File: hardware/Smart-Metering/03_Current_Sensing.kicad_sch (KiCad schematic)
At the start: 0 parts

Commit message: Implementa front-ends de tensão e corrente do ADE9430
02_Voltage_Sensing (3 fases, pseudo-diferencial):
- borne J101 (VA/VB/VC/VN) com labels globais LINE_A/B/C e NEUTRAL;
- fusível + varistor 320 VAC fase-neutro por fase;
- divisor 5 x 200 kΩ + 1 kΩ (1/1001): 220 V -> 0,311 Vpk, até ~354 Vrms
  com no máximo 0,5 Vpk por pino (limite do ADE9430: ±0,6 V);
- anti-aliasing 999 Ω // 22 nF (fc ≈ 7,2 kHz); VxN com 1 kΩ // 22 nF
  para casar impedância;
- R101 (0 Ω) liga NEUTRAL ao GND metrológico em ponto único.

03_Current_Sensing (IA/IB/IC/IN):
- entrada de TC por borne de 2 vias, TVS bidirecional SMAJ5.0CA;
- burden 2 x 10 Ω com center-tap no GND (TC 2500:1 -> fundo de escala
  ≈ 88 Arms, ±0,5 Vpk por pino);
- anti-aliasing 1 kΩ + 22 nF por perna (fc ≈ 7,2 kHz, casado com a tensão).

Biblioteca: novos símbolos Fuse, Varistor, D_TVS_Bi e
Screw_Terminal_01x02/01x04, já na convenção Y para cima do KiCad.

Co-Authored-By: Claude Opus 5.5 <noreply@anthropic.com>
Claude-Session: https://claude.ai/code/session_012B8cVkhtjf3eg98UdpNCpf
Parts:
- added C211, C212, C221, C222, C231, C232, C241, C242: 22nF C0G, Capacitor_SMD:C_0603_1608Metric, symbol SmartMetering:C_Vert
- added D201, D202, D203, D204: SMAJ5.0CA, Diode_SMD:D_SMA, symbol SmartMetering:D_TVS_Bi
- added J201: CT_IA, TerminalBlock_Phoenix:TerminalBlock_Phoenix_MKDS-1,5-2-5.08_1x02_P5.08mm_Horizontal, symbol SmartMetering:Screw_Terminal_01x02
- added J202: CT_IB, TerminalBlock_Phoenix:TerminalBlock_Phoenix_MKDS-1,5-2-5.08_1x02_P5.08mm_Horizontal, symbol SmartMetering:Screw_Terminal_01x02
- added J203: CT_IC, TerminalBlock_Phoenix:TerminalBlock_Phoenix_MKDS-1,5-2-5.08_1x02_P5.08mm_Horizontal, symbol SmartMetering:Screw_Terminal_01x02
- added J204: CT_IN, TerminalBlock_Phoenix:TerminalBlock_Phoenix_MKDS-1,5-2-5.08_1x02_P5.08mm_Horizontal, symbol SmartMetering:Screw_Terminal_01x02
- added R211, R212, R221, R222, R231, R232, R241, R242: 10R 0.1%, Resistor_SMD:R_1206_3216Metric, symbol SmartMetering:R_Vert
- added R213, R214, R223, R224, R233, R234, R243, R244: 1k 0.1%, Resistor_SMD:R_0603_1608Metric, symbol SmartMetering:R_Vert
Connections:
- new net: D202.1, J202.1, R221.1, R223.1
- new net: D202.2, J202.2, R222.2, R224.1
- new net: D203.1, J203.1, R231.1, R233.1
- new net: D203.2, J203.2, R232.2, R234.1
- new net: D201.2, J201.2, R212.2, R214.1
- new net: D204.1, J204.1, R241.1, R243.1
- new net: D204.2, J204.2, R242.2, R244.1
- new net: D201.1, J201.1, R211.1, R213.1
- new net GND: C211.1, C212.2, C221.1, C222.2, C231.1, C232.2, C241.1, C242.2, R211.2, R212.1, R221.2, R222.1, R231.2, R232.1, R241.2, R242.1
- new net IAN: C212.1, R214.2
- new net IAP: C211.2, R213.2
- new net IBN: C222.1, R224.2
- new net IBP: C221.2, R223.2
- new net ICN: C232.1, R234.2
- new net ICP: C231.2, R233.2
- new net INN: C242.1, R244.2
- new net INP: C241.2, R243.2
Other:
- note added: "FRONT-END DE CORRENTE — TC COM SAÍDA EM CORRENTE, DIFERENCIAL TC de referência: 2500:1 (mesma relação do EVAL-ADE9430) Burden: 2 x 10 Ω com center-tap no GND -> sinais IxP/IxN em antifase Fundo de escala do ADC: ±1 Vpk diferencial = 0,707 Vrms 0,707 V / 20 Ω = 35,4 mA no secundário -> Ifs ≈ 88 Arms no primário No fundo de escala cada pino fica em ±0,5 Vpk (limite ±0,6 V) Outra faixa: Rb_total = 0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"
- note added: "IA"
- note added: "IB"
- note added: "IC"
- note added: "IN (opcional)"
- company: (none) -> Smart-Metering
- title: (none) -> Current Sensing - ADE9430 Front-End

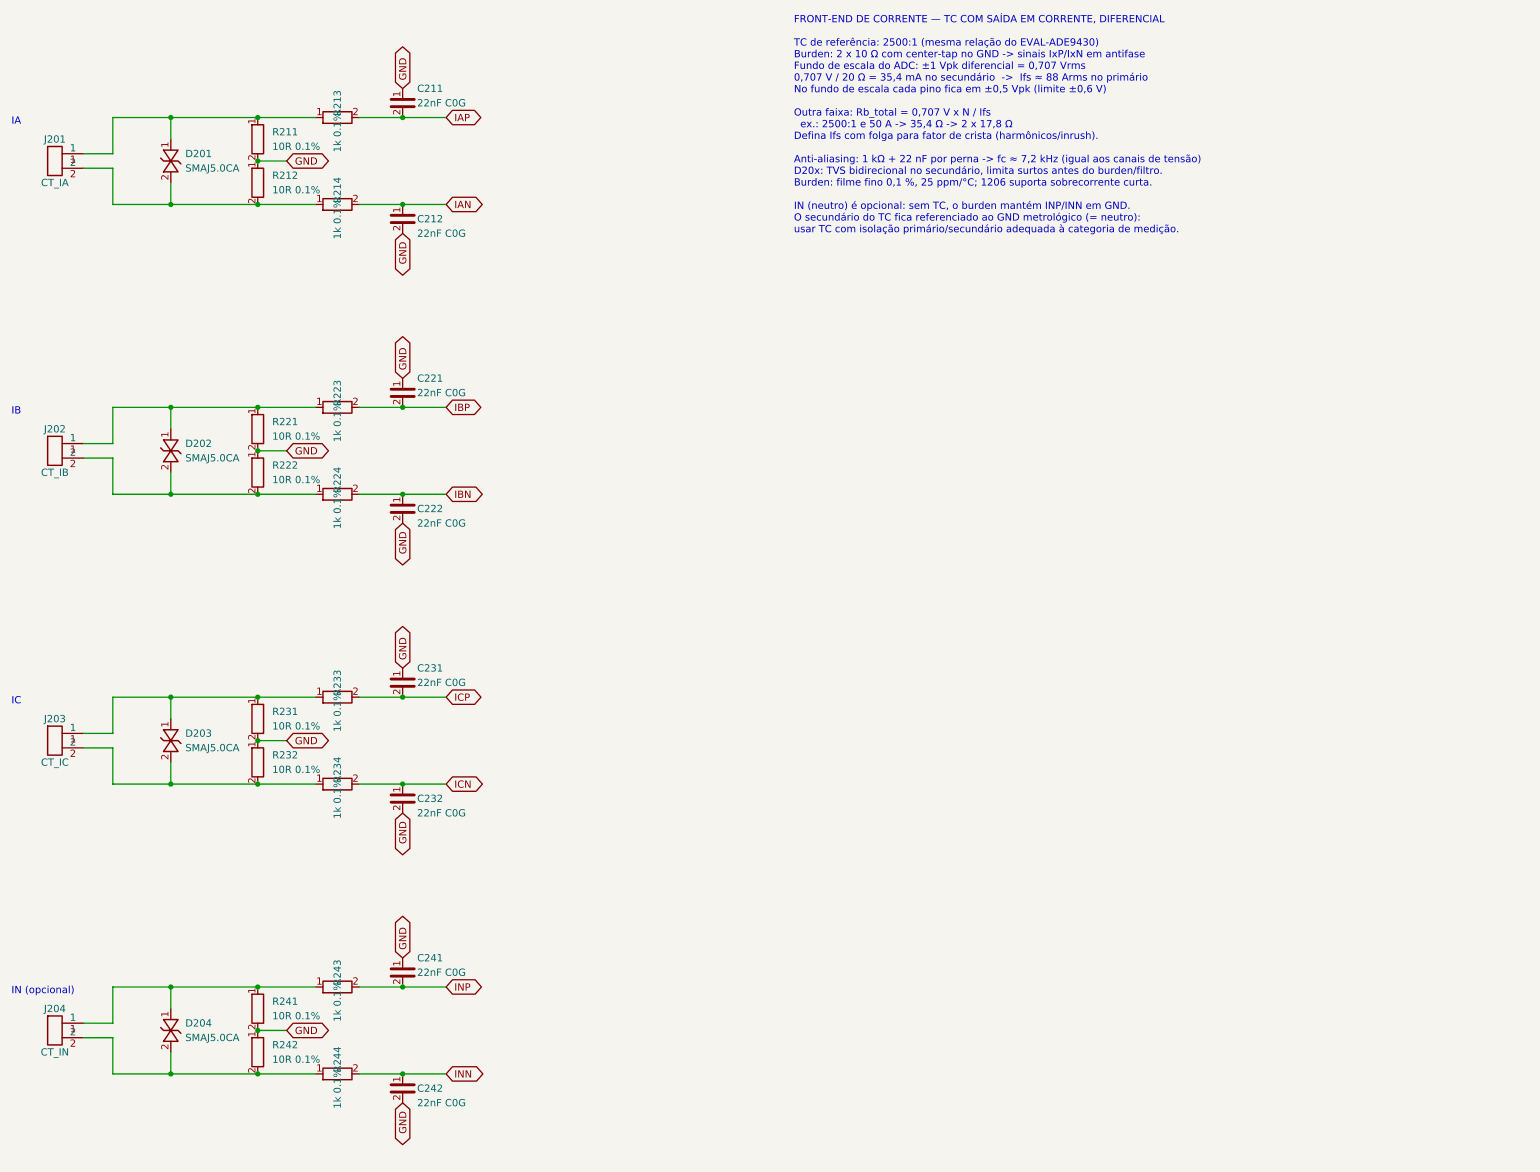
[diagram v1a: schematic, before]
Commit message: Refaz entrada de corrente para sensores configuráveis por montagem
A folha 03_Current_Sensing deixa de usar TC com saída em corrente
(risco de secundário aberto ao desconectar) e passa a aceitar, na
mesma placa, três tipos de sensor escolhidos pelos valores de Ra/Rb:

- TC 333 mV (padrão): Ra = 1k, Rb = 1M, ADE9430 com PGA 1x;
- bobina Rogowski: Ra = 1k, Rb = 1M, PGA 4x e integrador digital;
- SCT-013 com saída de 1 V (protótipo): Ra = 2k49, Rb = 1k65 (x0,40).

Em todas as opções Ra // Rb ≈ 1 kΩ, mantendo o anti-aliasing de
7,2 kHz com 22 nF, casado com os canais de tensão. Rb para GND em cada
perna referencia o sensor flutuante de forma simétrica.

Conector do sensor com 4 vias (S+, ID, GND, S-): o pino ID recebe um
pull-up de 10 kΩ para +3V3_ADE e filtro de 100 nF, saindo como SID_x
para leitura no domínio metrológico (a definir em 06_Isolation).

Biblioteca: novo símbolo genérico Conn_01x04.

Co-Authored-By: Claude Opus 5.5 <noreply@anthropic.com>
Claude-Session: https://claude.ai/code/session_012B8cVkhtjf3eg98UdpNCpf
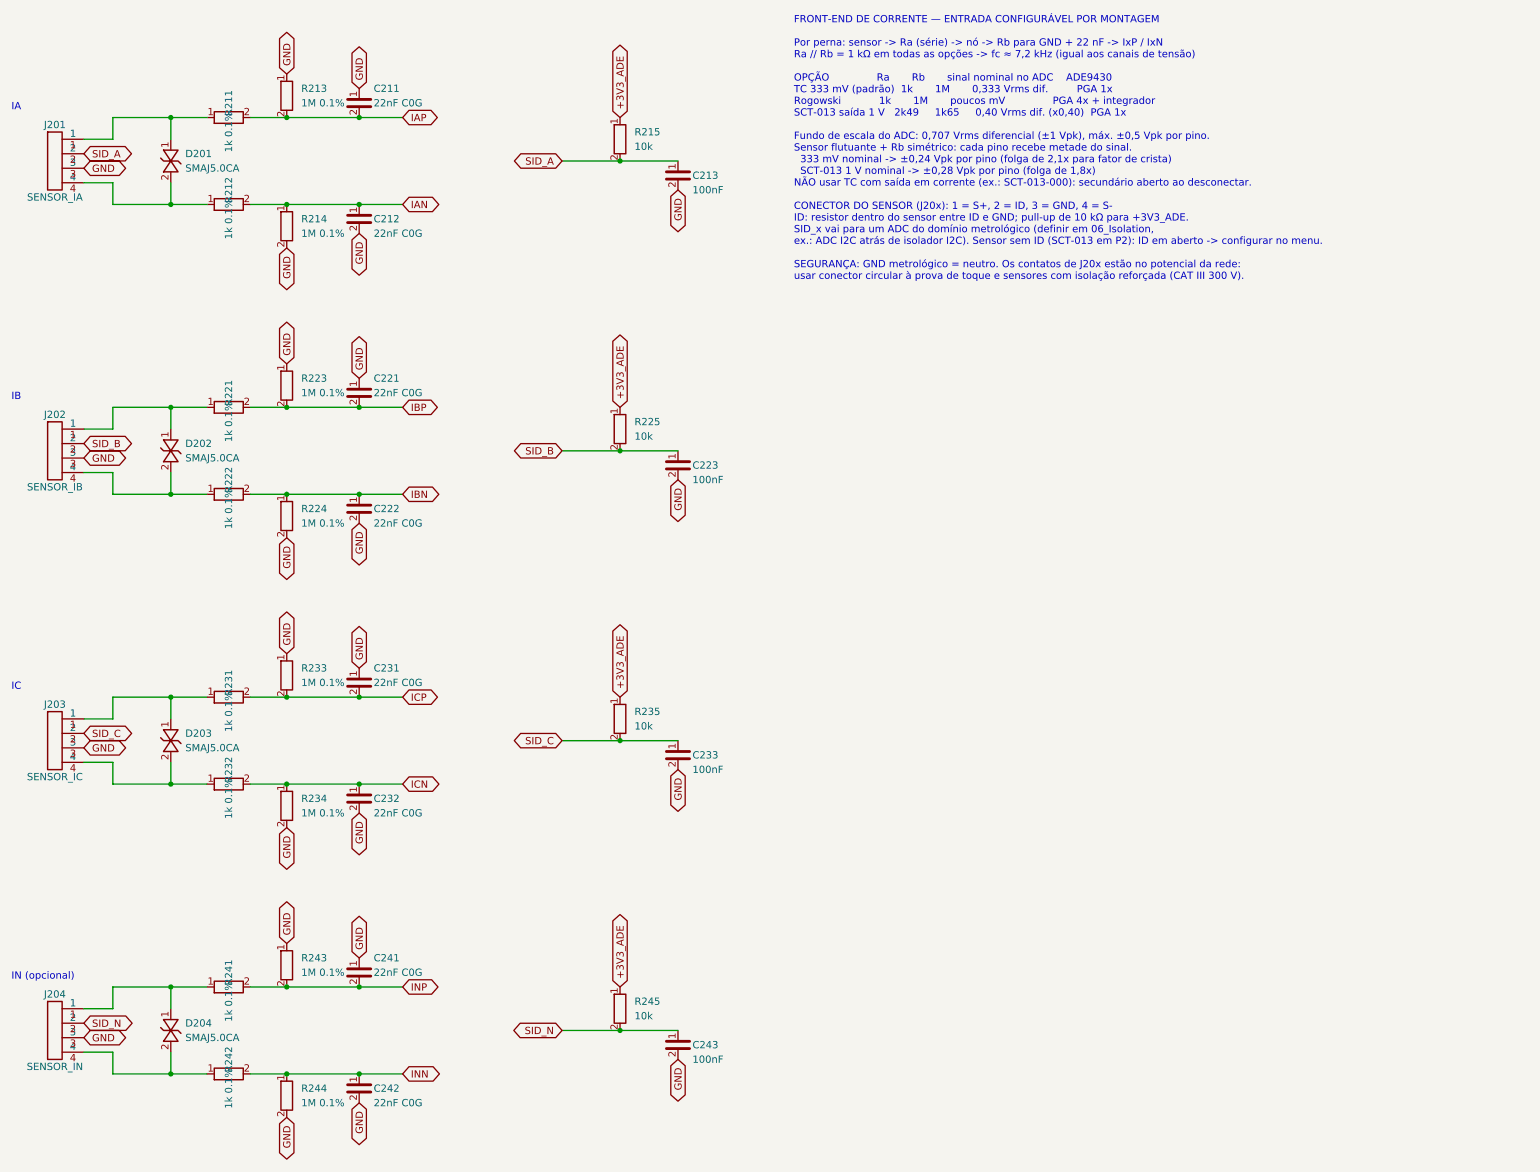
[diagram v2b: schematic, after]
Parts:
- removed J201: CT_IA, TerminalBlock_Phoenix:TerminalBlock_Phoenix_MKDS-1,5-2-5.08_1x02_P5.08mm_Horizontal, symbol SmartMetering:Screw_Terminal_01x02
- removed J202: CT_IB, TerminalBlock_Phoenix:TerminalBlock_Phoenix_MKDS-1,5-2-5.08_1x02_P5.08mm_Horizontal, symbol SmartMetering:Screw_Terminal_01x02
- removed J203: CT_IC, TerminalBlock_Phoenix:TerminalBlock_Phoenix_MKDS-1,5-2-5.08_1x02_P5.08mm_Horizontal, symbol SmartMetering:Screw_Terminal_01x02
- removed J204: CT_IN, TerminalBlock_Phoenix:TerminalBlock_Phoenix_MKDS-1,5-2-5.08_1x02_P5.08mm_Horizontal, symbol SmartMetering:Screw_Terminal_01x02
- added C213, C223, C233, C243: 100nF, Capacitor_SMD:C_0603_1608Metric, symbol SmartMetering:C_Vert
- added J201: SENSOR_IA, symbol SmartMetering:Conn_01x04
- added J202: SENSOR_IB, symbol SmartMetering:Conn_01x04
- added J203: SENSOR_IC, symbol SmartMetering:Conn_01x04
- added J204: SENSOR_IN, symbol SmartMetering:Conn_01x04
- added R215, R225, R235, R245: 10k, Resistor_SMD:R_0603_1608Metric, symbol SmartMetering:R_Vert
- R211, R212, R221, R222, R231, R232, R241, R242: value 10R 0.1% -> 1k 0.1%; footprint Resistor_SMD:R_1206_3216Metric -> Resistor_SMD:R_0603_1608Metric
- R213, R214, R223, R224, R233, R234, R243, R244: value 1k 0.1% -> 1M 0.1%
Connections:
- net GND: now also R213.1, R214.2, R223.1, R224.2, R233.1, R234.2, R243.1, R244.2, C213.2, C223.2, C233.2, C243.2, J201.3, J202.3, J203.3, J204.3; no longer R211.2, R212.1, R221.2, R222.1, R231.2, R232.1, R241.2, R242.1
- net IAN: now also R212.2, R214.1; no longer R214.2
- net IAP: now also R211.2
- net IBN: now also R222.2, R224.1; no longer R224.2
- net IBP: now also R221.2
- net ICN: now also R232.2, R234.1; no longer R234.2
- net ICP: now also R231.2
- net INN: now also R242.2, R244.1; no longer R244.2
- net INP: now also R241.2
- net at D202.1, R221.1: now also J202.1; no longer R223.1
- net at D203.1, R231.1: now also J203.1; no longer R233.1
- net at D204.1, R241.1: now also J204.1; no longer R243.1
- net at D201.1, R211.1: now also J201.1; no longer R213.1
- new net: D203.2, J203.4, R232.1
- new net: D204.2, J204.4, R242.1
- new net: D202.2, J202.4, R222.1
- new net: D201.2, J201.4, R212.1
- new net +3V3_ADE: R215.1, R225.1, R235.1, R245.1
- new net SID_A: C213.1, J201.2, R215.2
- new net SID_B: C223.1, J202.2, R225.2
- new net SID_C: C233.1, J203.2, R235.2
- new net SID_N: C243.1, J204.2, R245.2
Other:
- note added: "FRONT-END DE CORRENTE — ENTRADA CONFIGURÁVEL POR MONTAGEM Por perna: sensor -> Ra (série) -> nó -> Rb para GND + 22 nF -> IxP / IxN Ra // Rb = 1 kΩ em todas as opções -> fc ≈ 7,2 kHz (igual aos canais de tensão) OPÇÃO Ra Rb sinal nominal no ADC ADE9430 TC 333 mV (padrão) 1k 1M 0,333 Vrms dif. PGA 1x Rogowski 1k 1M poucos mV PGA 4x + integrador SCT-013 saída 1 V 2k49 1k65 0,40 Vrms dif. (x0,40) PG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"
- note removed: "FRONT-END DE CORRENTE — TC COM SAÍDA EM CORRENTE, DIFERENCIAL TC de referência: 2500:1 (mesma relação do EVAL-ADE9430) Burden: 2 x 10 Ω com center-tap no GND -> sinais IxP/IxN em antifase Fundo de escala do ADC: ±1 Vpk diferencial = 0,707 Vrms 0,707 V / 20 Ω = 35,4 mA no secundário -> Ifs ≈ 88 Arms no primário No fundo de escala cada pino fica em ±0,5 Vpk (limite ±0,6 V) Outra faixa: Rb_total = 0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"

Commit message: Implementa folha de entrada de energia e numera referências por folha
01_Power_Input:
- modo padrão: LINE_A/B/C -> fusível -> diodo S1M em OU para o
  barramento HV, retorno no NEUTRAL via JP101; o instrumento segue
  alimentado com qualquer fase presente;
- modo auxiliar (J101, 100-240 VAC, com varistor): F104/D104/JP102,
  não montados por padrão; para rede 3 fios sem neutro;
- R101 fusível limita inrush, C101 4,7 uF/450 V no barramento;
- PS101 módulo AC/DC isolado 5 V / 2 A (ex.: IRM-10-5) gerando
  VIN_ACDC para a folha 09, referenciado a GND_SYS.

Referências renumeradas por folha para evitar colisões: folha 02 passa
a 2xx (R201 = ligação neutro/GND), folha 03 a 3xx e folha 04 a 4xx
(U401 = ADE9430).

Novos símbolos: D_Rect, CP_Vert, Jumper_2 e ACDC_Module.

Co-Authored-By: Claude Opus 5.5 <noreply@anthropic.com>
Claude-Session: https://claude.ai/code/session_012B8cVkhtjf3eg98UdpNCpf
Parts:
- removed C211, C212, C221, C222, C231, C232, C241, C242: 22nF C0G, Capacitor_SMD:C_0603_1608Metric, symbol SmartMetering:C_Vert
- removed C213, C223, C233, C243: 100nF, Capacitor_SMD:C_0603_1608Metric, symbol SmartMetering:C_Vert
- removed D201, D202, D203, D204: SMAJ5.0CA, Diode_SMD:D_SMA, symbol SmartMetering:D_TVS_Bi
- removed J201: SENSOR_IA, symbol SmartMetering:Conn_01x04
- removed J202: SENSOR_IB, symbol SmartMetering:Conn_01x04
- removed J203: SENSOR_IC, symbol SmartMetering:Conn_01x04
- removed J204: SENSOR_IN, symbol SmartMetering:Conn_01x04
- removed R211, R212, R221, R222, R231, R232, R241, R242: 1k 0.1%, Resistor_SMD:R_0603_1608Metric, symbol SmartMetering:R_Vert
- removed R213, R214, R223, R224, R233, R234, R243, R244: 1M 0.1%, Resistor_SMD:R_0603_1608Metric, symbol SmartMetering:R_Vert
- removed R215, R225, R235, R245: 10k, Resistor_SMD:R_0603_1608Metric, symbol SmartMetering:R_Vert
- added C311, C312, C321, C322, C331, C332, C341, C342: 22nF C0G, Capacitor_SMD:C_0603_1608Metric, symbol SmartMetering:C_Vert
- added C313, C323, C333, C343: 100nF, Capacitor_SMD:C_0603_1608Metric, symbol SmartMetering:C_Vert
- added D301, D302, D303, D304: SMAJ5.0CA, Diode_SMD:D_SMA, symbol SmartMetering:D_TVS_Bi
- added J301: SENSOR_IA, symbol SmartMetering:Conn_01x04
- added J302: SENSOR_IB, symbol SmartMetering:Conn_01x04
- added J303: SENSOR_IC, symbol SmartMetering:Conn_01x04
- added J304: SENSOR_IN, symbol SmartMetering:Conn_01x04
- added R311, R312, R321, R322, R331, R332, R341, R342: 1k 0.1%, Resistor_SMD:R_0603_1608Metric, symbol SmartMetering:R_Vert
- added R313, R314, R323, R324, R333, R334, R343, R344: 1M 0.1%, Resistor_SMD:R_0603_1608Metric, symbol SmartMetering:R_Vert
- added R315, R325, R335, R345: 10k, Resistor_SMD:R_0603_1608Metric, symbol SmartMetering:R_Vert
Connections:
- net +3V3_ADE: now also R315.1, R325.1, R335.1, R345.1
- net GND: now also C311.1, C312.2, C313.2, C321.1, C322.2, C323.2, C331.1, C332.2, C333.2, C341.1, C342.2, C343.2, J301.3, J302.3, J303.3, J304.3, R313.1, R314.2, R323.1, R324.2, R333.1, R334.2, R343.1, R344.2
- net IAN: now also C312.1, R312.2, R314.1
- net IAP: now also C311.2, R311.2, R313.2
- net IBN: now also C322.1, R322.2, R324.1
- net IBP: now also C321.2, R321.2, R323.2
- net ICN: now also C332.1, R332.2, R334.1
- net ICP: now also C331.2, R331.2, R333.2
- net INN: now also C342.1, R342.2, R344.1
- net INP: now also C341.2, R341.2, R343.2
- net SID_A: now also C313.1, J301.2, R315.2
- net SID_B: now also C323.1, J302.2, R325.2
- net SID_C: now also C333.1, J303.2, R335.2
- net SID_N: now also C343.1, J304.2, R345.2
- new net: D304.2, J304.4, R342.1
- new net: D301.2, J301.4, R312.1
- new net: D302.2, J302.4, R322.1
- new net: D301.1, J301.1, R311.1
- new net: D303.1, J303.1, R331.1
- new net: D303.2, J303.4, R332.1
- new net: D302.1, J302.1, R321.1
- new net: D304.1, J304.1, R341.1
